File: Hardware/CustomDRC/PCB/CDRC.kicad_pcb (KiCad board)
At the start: 2 copper layers, 85 x 40 mm, 81 parts, among them IC301 SN65HVD75DR, J101 DSP Header, J401 TC2030NL - For UART PROG, J501 JST_PH_S5B-PH-SM4, J502 ST_PH_S2B-PH-SM4, J504 JST_PH_S5B-PH-SM4, Q501 AO3400A, U201 AP63203WU-7, U401 ESP32-WROOM-32UE-R2, U501 ESD224DQA, U502 ESD224DQA

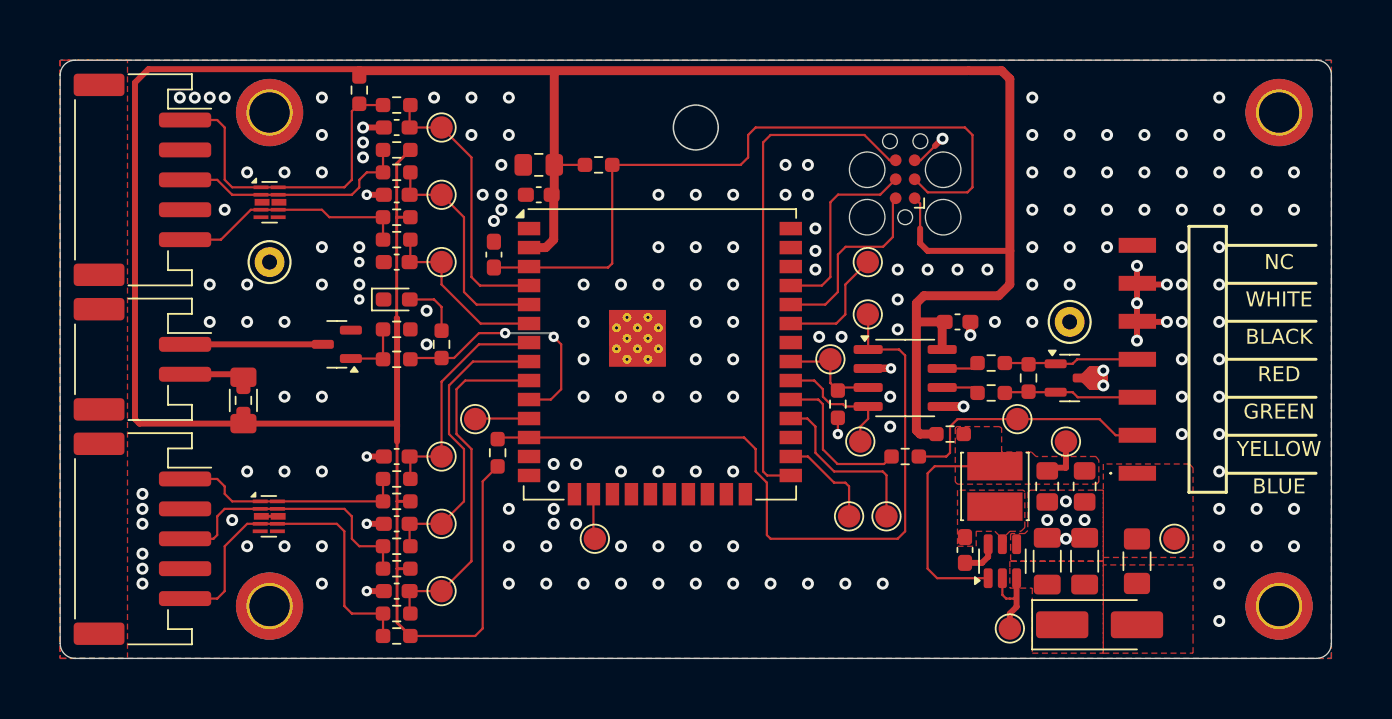
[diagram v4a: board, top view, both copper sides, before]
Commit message: Added board renders and PDF plots
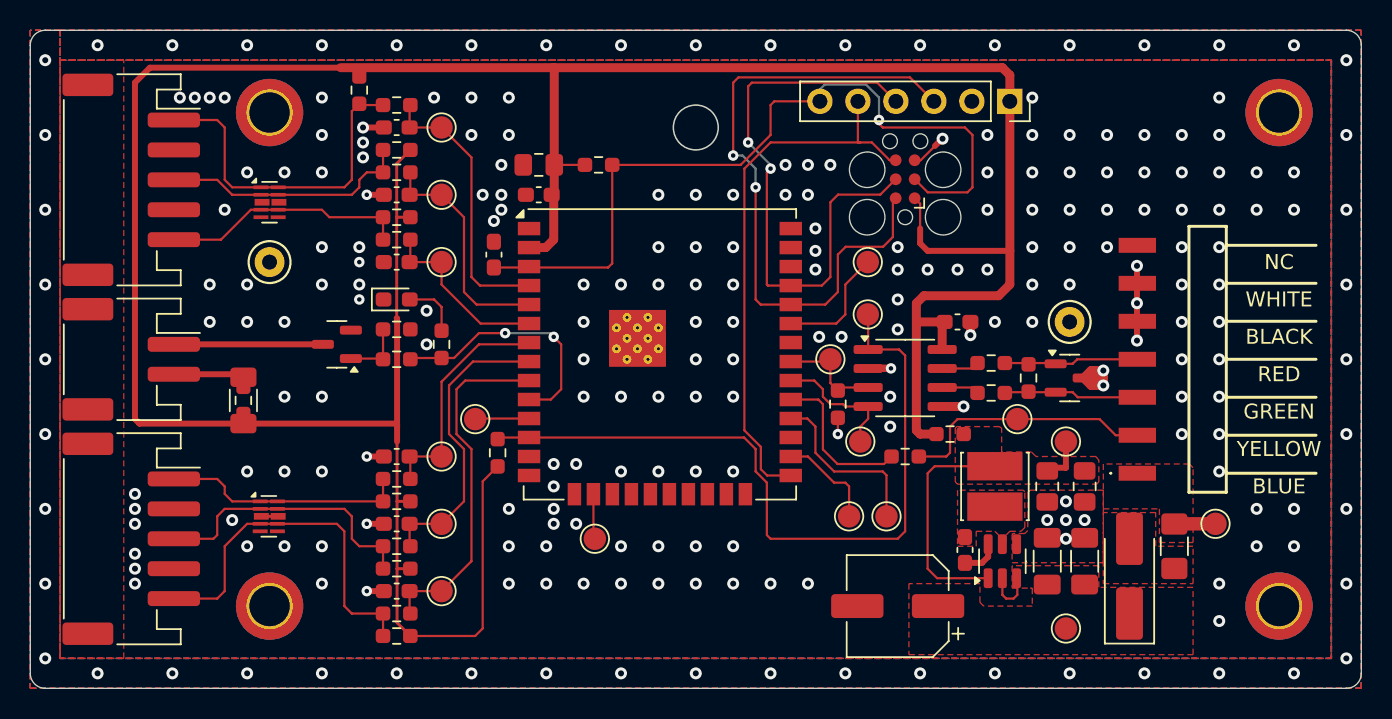
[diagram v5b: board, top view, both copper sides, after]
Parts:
- added C206: 22u, Capacitor_SMD:CP_Elec_6.3x5.4_Nichicon, F.Cu at (164.5, 114.8)
- added J301: Conn_01x06, Connector_PinSocket_2.54mm:PinSocket_1x06_P2.54mm_Vertical, F.Cu at (172.0, 81.0)
- moved D202 3.82 mm to (180.0, 112.8), turned to 90 degrees
- moved TP204 3.75 mm to (175.8, 116.2)
- moved TP102 2.93 mm to (185.8, 109.2)
- moved F201 2.69 mm to (183.0, 110.8)
- moved J501 0.75 mm to (113.2, 110.2)
- moved J502 0.75 mm to (113.2, 98.2)
- moved J504 0.75 mm to (113.2, 86.2)
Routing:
- net /MCU/ESP_RXD0: track 12.6 -> 44.8 mm, vias 0 -> 2
- net /MCU/ESP_TXD0: track 12.9 -> 39.0 mm, vias 0 -> 2
- net /MCU/ESP_EN: track 48.7 -> 52.9 mm, vias 0 -> 1
- net GND: track 27.1 -> 23.3 mm, vias 192 -> 243
- net Net-(D202-K): track 6.93 -> 3.38 mm
- net /MCU/ESP_BOOT0: track 33.7 -> 37.0 mm
- net /DSP_CONST_12V: track 0.00 -> 2.74 mm
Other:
- board size 85 x 40 mm -> 89 x 44 mm
- board text added: "BOOT"
- board text added: "DO NOT PLACE COMPONENTS MARKED"
- board text added: "EN"
- board text added: "RX"
- board text added: "TO303"
- board text added: "TP101"
- board text added: "TP102"
- board text added: "TP103"
- board text added: "TP203"
- board text added: "TP204"
- board text added: "TP301"
- board text added: "TP302"
- board text added: "TP304"
- board text added: "TP305"
- board text added: "TP306"
- board text added: "TP307"
- board text added: "TP308"
- board text added: "TP501"
- board text added: "TP502"
- board text added: "TP503"
- board text added: "TP504"
- board text added: "TP505"
- board text added: "TP506"
- board text added: "TP508"
- board text added: "TX"
- board text added: "VCC"
- board text added: "X"
- board text added: "Y"

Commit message: Update HW folder with latest work on rev B
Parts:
- added G***: LOGO, CDRC_Footprints:qr_code, B.Cu at (165.0, 107.5)
- added REF**: MountingHole_3.5mm, MountingHole:MountingHole_3.5mm, F.Cu at (151.0, 82.8)
- C206: value 22u -> 100U; footprint Capacitor_SMD:CP_Elec_6.3x5.4_Nichicon -> CDRC_Footprints:Capacitor_D6.3xL12mm_SMD
- J401: value TC2030NL - For UART PROG -> TC2030NL
- J502: value ST_PH_S2B-PH-SM4 -> JST_PH_S2B-PH-SM4
- moved C206 0.50 mm to (164.5, 114.2), turned to 0 degrees
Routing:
- net GND: track 23.3 -> 26.0 mm, vias 243 -> 248
- net /MCU/ESP_TXD0: track 39.0 -> 40.4 mm
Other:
- outline, holes or cut-outs redrawn
- board text added: "ANTENNA"
- board text removed: "ANT"
